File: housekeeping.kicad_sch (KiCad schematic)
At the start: 20 parts

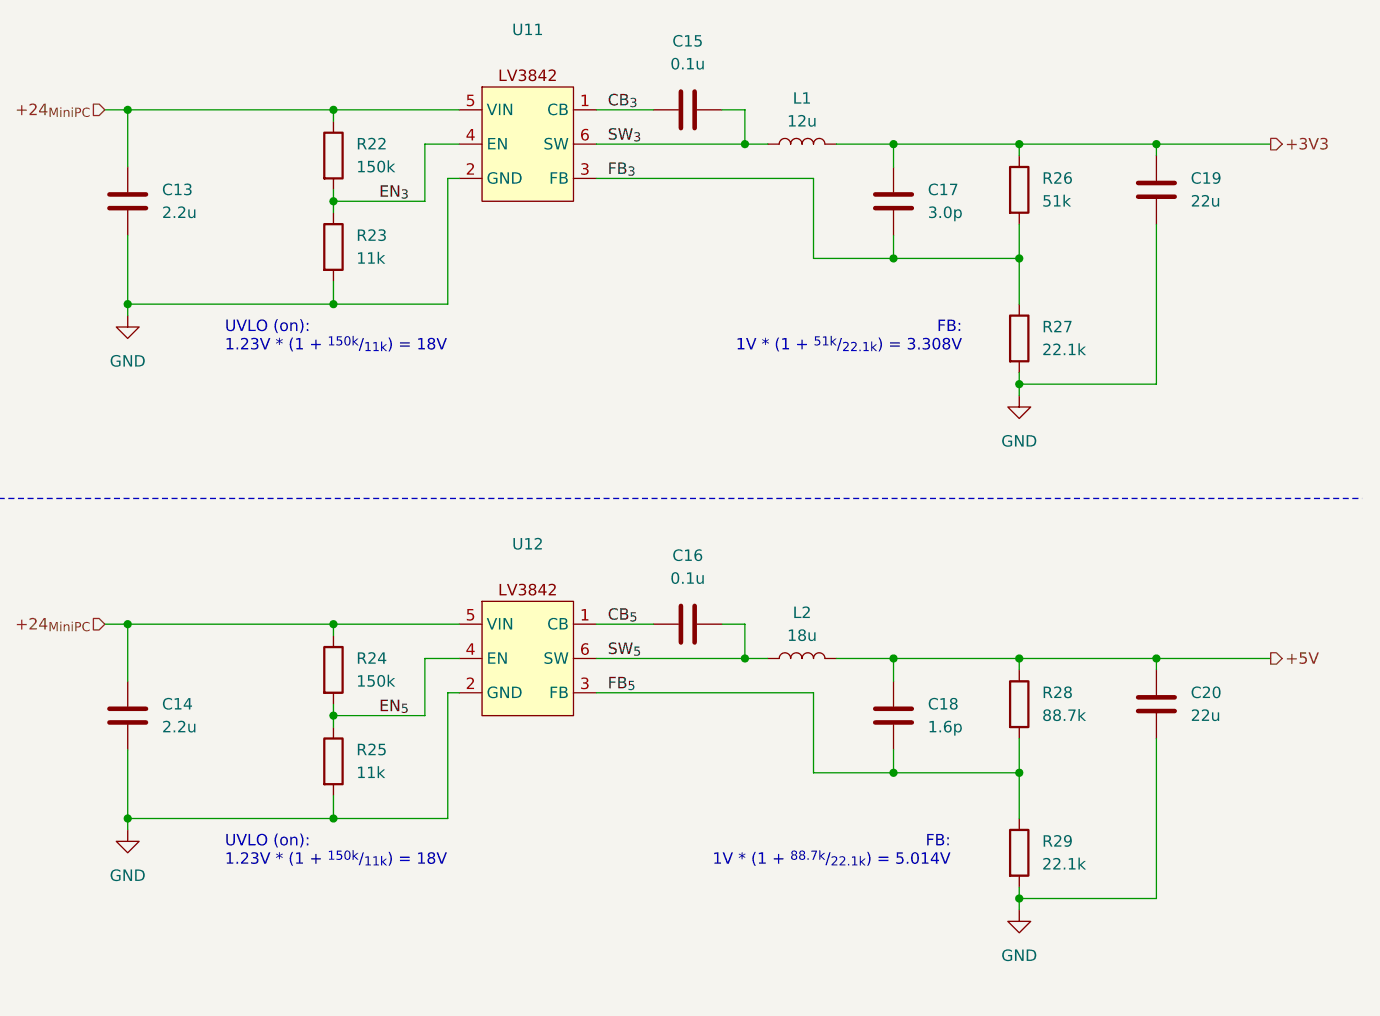
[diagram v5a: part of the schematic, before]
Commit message: Add input resistor divider to battery voltage ADC
+ renumbered components
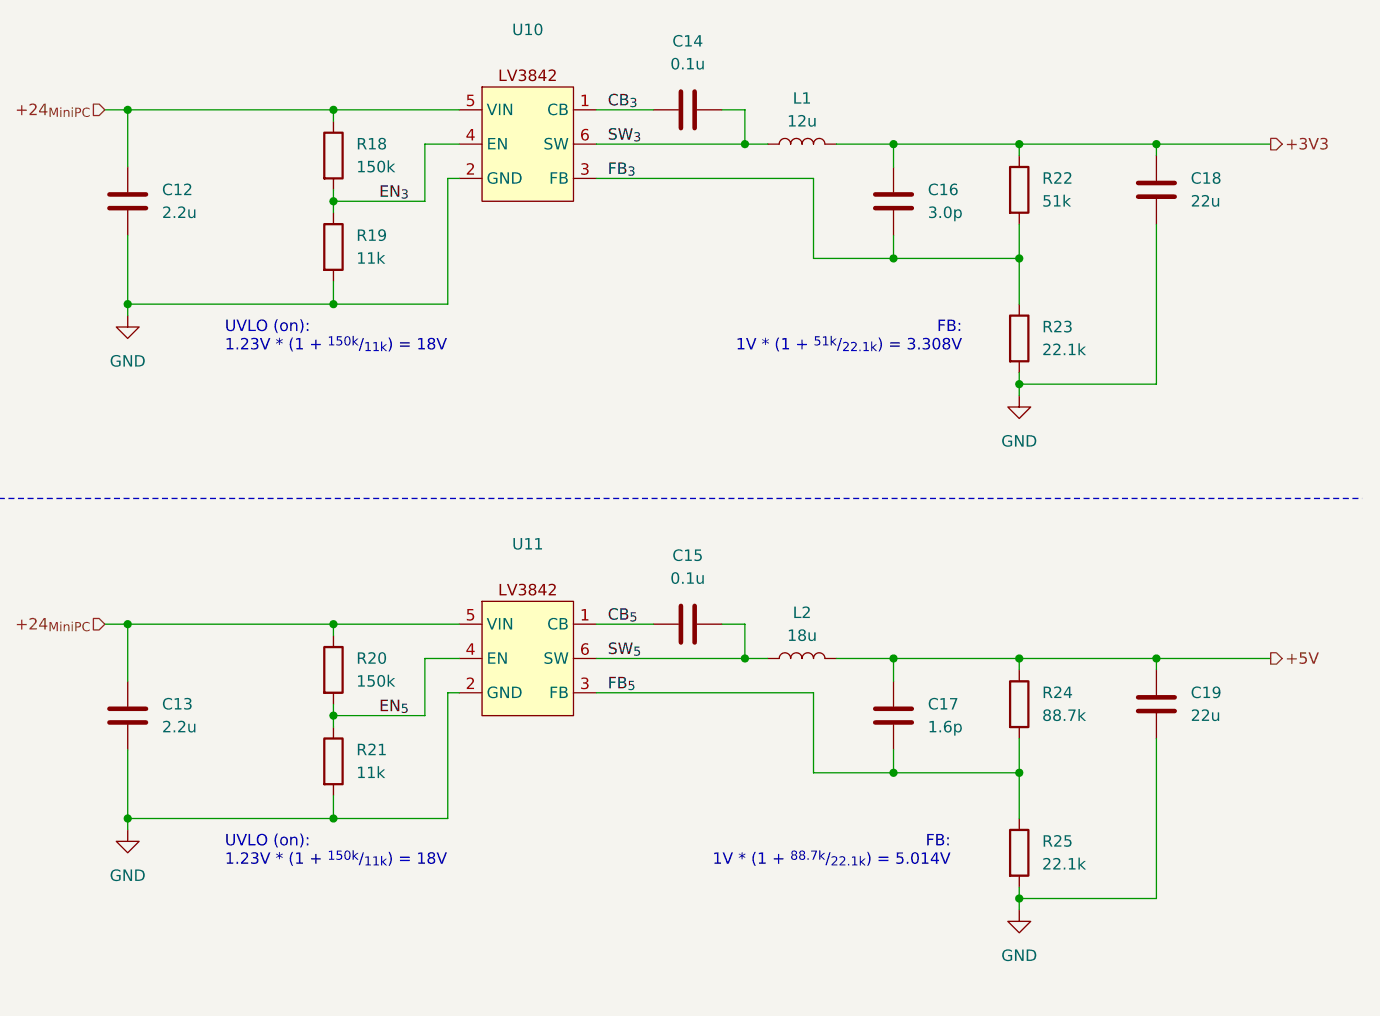
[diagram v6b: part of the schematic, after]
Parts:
- renumbered C13 to C12, C14 to C13, C15 to C14, C16 to C15, C17 to C16, C18 to C17, C19 to C18, C20 to C19, R22 to R18, R23 to R19, R24 to R20, R25 to R21, R26 to R22, R27 to R23, R28 to R24, R29 to R25, U11 to U10, U12 to U11
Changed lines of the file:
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@@
 		(dnp no)
 		(fields_autoplaced yes)
-		(property "Reference" "R22"
+		(property "Reference" "R18"
 			(at 113.03 53.3399 0)
 			(effects
@@
 			(project ""
 				(path "/6197145b-e7d4-44cc-9d90-537b6501bf60/2b4de7d2-e111-42d9-afee-f810f96a2f61"
-					(reference "R22")
+					(reference "R18")
 					(unit 1)
 				)
@@
 		(dnp no)
 		(fields_autoplaced yes)
-		(property "Reference" "C19"
+		(property "Reference" "C18"
 			(at 205.74 57.1499 0)
 			(effects
@@
 			(project ""
 				(path "/6197145b-e7d4-44cc-9d90-537b6501bf60/2b4de7d2-e111-42d9-afee-f810f96a2f61"
-					(reference "C19")
+					(reference "C18")
 					(unit 1)
 				)
@@
 		(dnp no)
 		(fields_autoplaced yes)
-		(property "Reference" "#PWR047"
+		(property "Reference" "#PWR045"
 			(at 87.63 78.74 0)
 			(effects
@@
 			(project ""
 				(path "/6197145b-e7d4-44cc-9d90-537b6501bf60/2b4de7d2-e111-42d9-afee-f810f96a2f61"
-					(reference "#PWR047")
+					(reference "#PWR045")
 					(unit 1)
 				)
@@
 		(dnp no)
 		(fields_autoplaced yes)
-		(property "Reference" "#PWR050"
+		(property "Reference" "#PWR048"
 			(at 186.69 144.78 0)
 			(effects
@@
 			(project "SupercapManager"
 				(path "/6197145b-e7d4-44cc-9d90-537b6501bf60/2b4de7d2-e111-42d9-afee-f810f96a2f61"
-					(reference "#PWR050")
+					(reference "#PWR048")
 					(unit 1)
 				)
@@
 		(dnp no)
 		(fields_autoplaced yes)
-		(property "Reference" "#PWR048"
+		(property "Reference" "#PWR046"
 			(at 87.63 135.89 0)
 			(effects
@@
 			(project "SupercapManager"
 				(path "/6197145b-e7d4-44cc-9d90-537b6501bf60/2b4de7d2-e111-42d9-afee-f810f96a2f61"
-					(reference "#PWR048")
+					(reference "#PWR046")
 					(unit 1)
 				)
@@
 		(dnp no)
 		(fields_autoplaced yes)
-		(property "Reference" "R28"
+		(property "Reference" "R24"
 			(at 189.23 114.2999 0)
 			(effects
@@
 			(project "SupercapManager"
 				(path "/6197145b-e7d4-44cc-9d90-537b6501bf60/2b4de7d2-e111-42d9-afee-f810f96a2f61"
-					(reference "R28")
+					(reference "R24")
 					(unit 1)
 				)
@@
 		(dnp no)
 		(fields_autoplaced yes)
-		(property "Reference" "R29"
+		(property "Reference" "R25"
 			(at 189.23 130.8099 0)
 			(effects
@@
 			(project "SupercapManager"
 				(path "/6197145b-e7d4-44cc-9d90-537b6501bf60/2b4de7d2-e111-42d9-afee-f810f96a2f61"
-					(reference "R29")
+					(reference "R25")
 					(unit 1)
 				)
@@
 		(dnp no)
 		(fields_autoplaced yes)
-		(property "Reference" "C18"
+		(property "Reference" "C17"
 			(at 176.53 115.5699 0)
 			(effects
@@
 			(project "SupercapManager"
 				(path "/6197145b-e7d4-44cc-9d90-537b6501bf60/2b4de7d2-e111-42d9-afee-f810f96a2f61"
-					(reference "C18")
+					(reference "C17")
 					(unit 1)
 				)
@@
 		(dnp no)
 		(fields_autoplaced yes)
-		(property "Reference" "R24"
+		(property "Reference" "R20"
 			(at 113.03 110.4899 0)
 			(effects
@@
 			(project "SupercapManager"
 				(path "/6197145b-e7d4-44cc-9d90-537b6501bf60/2b4de7d2-e111-42d9-afee-f810f96a2f61"
-					(reference "R24")
+					(reference "R20")
 					(unit 1)
 				)
@@
 		(dnp no)
 		(fields_autoplaced yes)
-		(property "Reference" "U12"
+		(property "Reference" "U11"
 			(at 132.08 97.79 0)
 			(effects
@@
 			(project "SupercapManager"
 				(path "/6197145b-e7d4-44cc-9d90-537b6501bf60/2b4de7d2-e111-42d9-afee-f810f96a2f61"
-					(reference "U12")
+					(reference "U11")
 					(unit 1)
 				)
@@
 		(dnp no)
 		(fields_autoplaced yes)
-		(property "Reference" "C20"
+		(property "Reference" "C19"
 			(at 205.74 114.2999 0)
 			(effects
@@
 			(project "SupercapManager"
 				(path "/6197145b-e7d4-44cc-9d90-537b6501bf60/2b4de7d2-e111-42d9-afee-f810f96a2f61"
-					(reference "C20")
+					(reference "C19")
 					(unit 1)
 				)
@@
 		(dnp no)
 		(fields_autoplaced yes)
-		(property "Reference" "C16"
+		(property "Reference" "C15"
 			(at 149.86 99.06 90)
 			(effects
@@
 			(project "SupercapManager"
 				(path "/6197145b-e7d4-44cc-9d90-537b6501bf60/2b4de7d2-e111-42d9-afee-f810f96a2f61"
-					(reference "C16")
+					(reference "C15")
 					(unit 1)
 				)
@@
 		(dnp no)
 		(fields_autoplaced yes)
-		(property "Reference" "C17"
+		(property "Reference" "C16"
 			(at 176.53 58.4199 0)
 			(effects
@@
 			(project "SupercapManager"
 				(path "/6197145b-e7d4-44cc-9d90-537b6501bf60/2b4de7d2-e111-42d9-afee-f810f96a2f61"
-					(reference "C17")
+					(reference "C16")
 					(unit 1)
 				)
@@
 		(dnp no)
 		(fields_autoplaced yes)
-		(property "Reference" "U11"
+		(property "Reference" "U10"
 			(at 132.08 40.64 0)
 			(effects
@@
 			(project ""
 				(path "/6197145b-e7d4-44cc-9d90-537b6501bf60/2b4de7d2-e111-42d9-afee-f810f96a2f61"
-					(reference "U11")
+					(reference "U10")
 					(unit 1)
 				)
@@
 		(dnp no)
 		(fields_autoplaced yes)
-		(property "Reference" "R25"
+		(property "Reference" "R21"
 			(at 113.03 120.6499 0)
 			(effects
@@
 			(project "SupercapManager"
 				(path "/6197145b-e7d4-44cc-9d90-537b6501bf60/2b4de7d2-e111-42d9-afee-f810f96a2f61"
-					(reference "R25")
+					(reference "R21")
 					(unit 1)
 				)
@@
 		(dnp no)
 		(fields_autoplaced yes)
-		(property "Reference" "R27"
+		(property "Reference" "R23"
 			(at 189.23 73.6599 0)
 			(effects
@@
 			(project "SupercapManager"
 				(path "/6197145b-e7d4-44cc-9d90-537b6501bf60/2b4de7d2-e111-42d9-afee-f810f96a2f61"
-					(reference "R27")
+					(reference "R23")
 					(unit 1)
 				)
@@
 		(dnp no)
 		(fields_autoplaced yes)
-		(property "Reference" "C14"
+		(property "Reference" "C13"
 			(at 91.44 115.5699 0)
 			(effects
@@
 			(project "SupercapManager"
 				(path "/6197145b-e7d4-44cc-9d90-537b6501bf60/2b4de7d2-e111-42d9-afee-f810f96a2f61"
-					(reference "C14")
+					(reference "C13")
 					(unit 1)
 				)
@@
 		(dnp no)
 		(fields_autoplaced yes)
-		(property "Reference" "R23"
+		(property "Reference" "R19"
 			(at 113.03 63.4999 0)
 			(effects
@@
 			(project "SupercapManager"
 				(path "/6197145b-e7d4-44cc-9d90-537b6501bf60/2b4de7d2-e111-42d9-afee-f810f96a2f61"
-					(reference "R23")
+					(reference "R19")
 					(unit 1)
 				)
@@
 		(dnp no)
 		(fields_autoplaced yes)
-		(property "Reference" "#PWR049"
+		(property "Reference" "#PWR047"
 			(at 186.69 87.63 0)
 			(effects
@@
 			(project "SupercapManager"
 				(path "/6197145b-e7d4-44cc-9d90-537b6501bf60/2b4de7d2-e111-42d9-afee-f810f96a2f61"
-					(reference "#PWR049")
+					(reference "#PWR047")
 					(unit 1)
 				)
@@
 		(dnp no)
 		(fields_autoplaced yes)
-		(property "Reference" "R26"
+		(property "Reference" "R22"
 			(at 189.23 57.1499 0)
 			(effects
@@
 			(project "SupercapManager"
 				(path "/6197145b-e7d4-44cc-9d90-537b6501bf60/2b4de7d2-e111-42d9-afee-f810f96a2f61"
-					(reference "R26")
+					(reference "R22")
 					(unit 1)
 				)
@@
 		(dnp no)
 		(fields_autoplaced yes)
-		(property "Reference" "C15"
+		(property "Reference" "C14"
 			(at 149.86 41.91 90)
 			(effects
@@
 			(project ""
 				(path "/6197145b-e7d4-44cc-9d90-537b6501bf60/2b4de7d2-e111-42d9-afee-f810f96a2f61"
-					(reference "C15")
+					(reference "C14")
 					(unit 1)
 				)
@@
 		(dnp no)
 		(fields_autoplaced yes)
-		(property "Reference" "C13"
+		(property "Reference" "C12"
 			(at 91.44 58.4199 0)
 			(effects
@@
 			(project ""
 				(path "/6197145b-e7d4-44cc-9d90-537b6501bf60/2b4de7d2-e111-42d9-afee-f810f96a2f61"
-					(reference "C13")
-					(unit 1)
-				)
+					(reference "C12")
+					(unit 1)
+				)
